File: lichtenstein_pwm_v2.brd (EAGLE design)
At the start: 71.9 x 117 mm, 94 parts, among them IC1 MAX11647, IC2 MCP23017, IC3 74AHCT125SOIC14, IC5 LM75B, IC9 LD1117, J1 MAGJACK, U1 ONION-OMEGA2

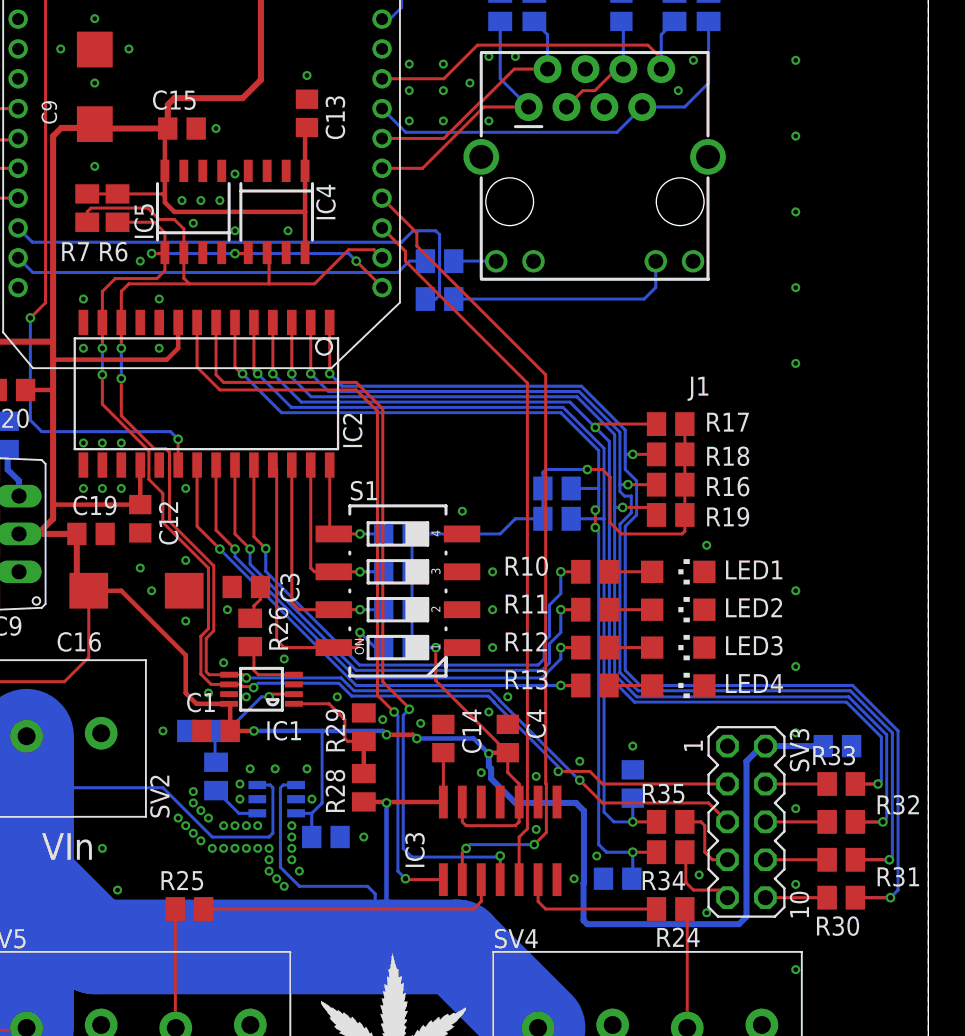
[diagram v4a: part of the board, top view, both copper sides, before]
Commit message: removed input connector, cleaned up some signals
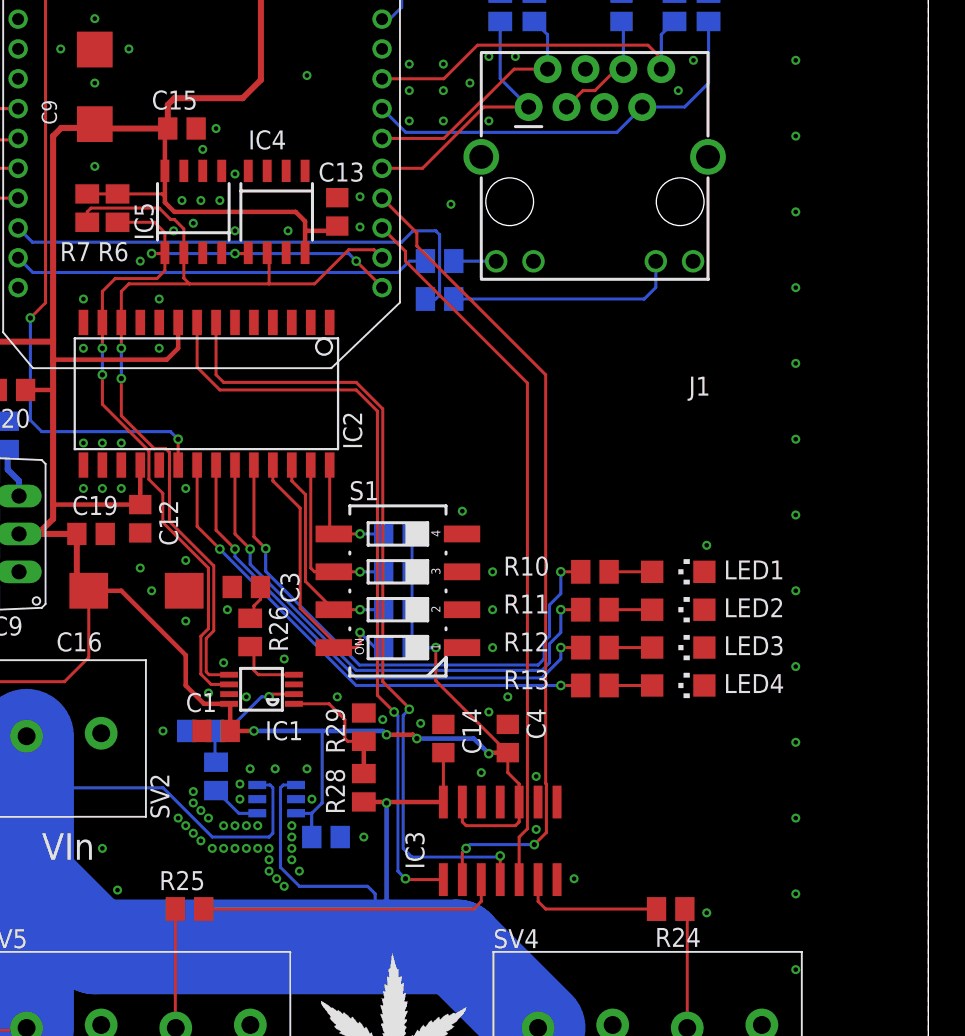
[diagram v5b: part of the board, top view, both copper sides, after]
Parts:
- removed C21, C22, C23, C24, C25, C26, C27: 100nF, rcl:C0805
- removed R16, R17, R18, R19, R20, R21, R30, R31, R32, R33, R34, R35: 10k, rcl:M0805
- removed SV3: (no value), con-lstb:MA05-2
- moved C13 6.91 mm to (32.3, 82.5)
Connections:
- removed net INPUT0: C21.2, IC2.2, R16.1, R31.2
- removed net INPUT1: C22.2, IC2.4, R17.1, R33.2
- removed net INPUT2: C23.2, IC2.6, R20.1, R34.2
- removed net INPUT3: C24.2, IC2.5, R21.1, R35.2
- removed net INPUT4: C25.2, IC2.1, R18.1, R30.2
- removed net INPUT5: C26.2, IC2.3, R19.1, R32.2
- removed net N$15: R30.1, SV3.10
- removed net N$16: R31.1, SV3.8
- removed net N$17: R32.1, SV3.6
- removed net N$18: R33.1, SV3.4
- removed net N$19: R34.1, SV3.9
- removed net N$20: R35.1, SV3.7
- net +3V3: no longer C27.2, IC4.1, R16.2, R17.2, R18.2, R19.2, R20.2, R21.2, SV3.2
- net GND: now also IC4.1; no longer C21.1, C22.1, C23.1, C24.1, C25.1, C26.1, C27.1, SV3.1
- net I2C_SCL: no longer SV3.5
- net I2C_SDA: no longer SV3.3
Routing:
- net +3V3: track 313.0 -> 232.8 mm, vias 6 -> 5
- net INPUT4: track 79.7 -> 0.00 mm, vias 3 -> 0
- net INPUT0: track 78.3 -> 0.00 mm, vias 3 -> 0
- net INPUT5: track 75.6 -> 0.00 mm, vias 3 -> 0
- net INPUT1: track 74.0 -> 0.00 mm, vias 3 -> 0
- net INPUT2: track 64.0 -> 0.00 mm, vias 4 -> 0
- net INPUT3: track 60.8 -> 0.00 mm, vias 2 -> 0
- net I2C_SCL: track 100.5 -> 63.0 mm, vias 4 -> 2
- net I2C_SDA: track 97.3 -> 60.7 mm, vias 7 -> 5
- net N$19: track 5.27 -> 0.00 mm
- net N$20: track 4.95 -> 0.00 mm
- net N$18: track 4.13 -> 0.00 mm
- net N$17: track 4.13 -> 0.00 mm
- net N$16: track 4.13 -> 0.00 mm
- net N$15: track 4.13 -> 0.00 mm
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
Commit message: more aesthetic fixes to board
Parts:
- moved C15 1.27 mm to (21.8, 89.4)
- moved C9 0.76 mm to (16.0, 91.7)
- moved R6 0.76 mm to (16.8, 82.8)
- moved R7 0.76 mm to (14.7, 82.8)
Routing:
- net +3V3: track 232.8 -> 231.4 mm
- net I2C_SDA: track 60.7 -> 61.4 mm
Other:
- board text added: "GND TX RX UART"

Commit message: more board clean-up
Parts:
- removed C28, C29, C30: 100nF, rcl:C0805
- removed R27: 1k2, rcl:M0805
- removed R28: 3k09, rcl:M0805
- removed R29: 1k07, rcl:M0805
- removed R36: 330R, rcl:M0805
- added C21, C24: 100nF, rcl:C0805
- added C22: 100µF, rcl:PANASONIC_D
- added C23: 100µF, rcl:CT7343
- added R16: 49.9R, rcl:M0805
- added R17, R18: 680R, rcl:M0805
- added R19: 330R, rcl:M0805
- added SV3: (no value), con-lstb:MA04-1
- C16: value 100µF -> 100nF; device rcl:CT7343 -> rcl:C0805
- C17: value 100µF -> 100nF; device rcl:PANASONIC_D -> rcl:C0805
- C4, C6: value 100nF -> 47µF; device rcl:C0805 -> rcl:SMC_C
- C5, C9: value 47µF -> 100nF; device rcl:SMC_C -> rcl:C0805
- IC1: value MAX11647 -> MCP23017; device lichtenstein_onion:UMAX8 -> lichtenstein_onion:SO28W
- IC2: value MCP23017 -> 74AHCT125SOIC14; device lichtenstein_onion:SO28W -> lichtenstein_onion:SO14
- IC3: value 74AHCT125SOIC14 -> MAX11647; device lichtenstein_onion:SO14 -> lichtenstein_onion:UMAX8
- R15: value 49.9R -> 1k2
- R22: value 680R -> 3k09
- R23: value 680R -> 1k07
- SV2: value 1792863 -> (none); device lichtenstein_onion:1792863 -> con-lstb:MA06-1
- SV6: value (none) -> 1792863; device con-lstb:MA06-1 -> lichtenstein_onion:1792863
- moved R15 79.5 mm to (5.33, 27.7), flipped to the top, turned to 180 degrees
- moved C7 78.2 mm to (44.2, 99.3), turned to 0 degrees
- moved C6 70.8 mm to (16.0, 91.7), flipped to the top, turned to 90 degrees
- moved C15 69.1 mm to (11.4, 21.1), flipped to the bottom, turned to 270 degrees
- moved C4 61.4 mm to (24.6, 105.7), turned to 180 degrees
- moved C3 50.0 mm to (40.1, 105.4)
- moved C11 49.6 mm to (43.7, 47.2), flipped to the top
- moved C16 44.9 mm to (45.5, 21.1), flipped to the bottom, turned to 270 degrees
- moved C10 44.3 mm to (10.4, 70.6), flipped to the top, turned to 180 degrees
- moved SV2 36.6 mm to (5.08, 83.6), turned to 90 degrees
- moved SV6 36.6 mm to (11.4, 47.5), turned to 0 degrees
- moved C14 36.0 mm to (32.3, 82.5)
- moved C13 35.7 mm to (24.1, 47.8), turned to 0 degrees
- moved R22 35.7 mm to (34.0, 43.9), flipped to the top, turned to 270 degrees
- moved IC2 35.5 mm to (43.2, 40.4), turned to 0 degrees
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- renumbered IC9 to IC7, R25 to R20, R26 to R21
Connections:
- net !PWM0_OE: now also IC1.8, IC2.1; no longer IC2.8, IC3.1
- net !PWM1_OE: now also IC1.7, IC2.4; no longer IC2.7, IC3.4
- net !SPI_CS: now also SV2.3; no longer SV6.3
- net +3V3: now also C1.1, C10.1, C11.2, C14.2, C18.2, C19.2, C23.+, C24.1, C3.1, C4.+, C6.+, C9.1, IC1.18, IC1.9, IC2.10, IC2.13, IC3.8, SV2.2, SV3.2; no longer C1.2, C12.1, C15.2, C16.+, C19.1, C20.1, C28.1, C29.2, C4.2, C5.+, C9.+, IC1.8, IC2.18, IC2.9, IC3.10, IC3.13, SV6.2
- net CURRENT: now also C20.1, IC3.2, R24.1; no longer C30.1, IC1.2, R36.1
- net ETH_CT: now also C8.2; no longer C11.2
- net ETH_LED_ACT: now also R17.2; no longer R22.2
- net ETH_LED_LINK: now also R18.2; no longer R23.2
- net ETH_RX-: now also R16.1; no longer R15.1
- net GND: now also C1.2, C10.2, C12.1, C15.2, C16.2, C17.1, C18.1, C19.1, C21.2, C22.-, C23.-, C24.2, C3.2, C4.-, C5.1, C6.-, C7.1, C9.2, IC1.10, IC1.15, IC1.16, IC1.17, IC2.12, IC2.7, IC2.9, R23.1, SV2.1, SV3.1, SV6.2; no longer C1.1, C10.1, C12.2, C15.1, C16.-, C17.-, C18.2, C19.2, C28.2, C29.1, C3.1, C30.2, C4.1, C5.-, C6.2, C7.2, C9.-, IC1.7, IC2.10, IC2.15, IC2.16, IC2.17, IC3.12, IC3.9, R29.1, SV2.2, SV6.1
- net I2C_INT: now also IC1.20; no longer IC2.20
- net I2C_SCL: now also IC1.12, IC3.5, SV3.3; no longer IC1.5, IC2.12
- net I2C_SDA: now also IC1.13, IC3.6, SV3.4; no longer IC1.6, IC2.13
- net N$12: now also IC3.4; no longer IC1.4
- net N$13: now also C17.2; no longer C3.2
- net N$14: now also R15.2; no longer R27.2
- net N$21: now also R24.2; no longer R36.2
- net N$3: now also C5.2; no longer C8.2
- net N$4: now also R17.1; no longer R22.1
- net N$5: now also R18.1; no longer R23.1
- net N$6: now also C7.2, R16.2; no longer C10.2, R15.2
- net N$7: now also R19.2; no longer R24.2
- net PWM0: now also IC2.2; no longer IC3.2
- net PWM1: now also IC2.5; no longer IC3.5
- net PWMOUT0: now also IC2.6, R19.1; no longer IC3.6, R24.1
- net PWMOUT1: now also IC2.3; no longer IC3.3
- net SPI_MISO: now also SV2.6; no longer SV6.6
- net SPI_MOSI: now also SV2.5; no longer SV6.5
- net SPI_SCK: now also SV2.4; no longer SV6.4
- net STATUS0: now also IC1.24; no longer IC2.24
- net STATUS1: now also IC1.23; no longer IC2.23
- net STATUS2: now also IC1.22; no longer IC2.22
- net STATUS3: now also IC1.21; no longer IC2.21
- net TEST0: now also IC1.25; no longer IC2.25
- net TEST1: now also IC1.26; no longer IC2.26
- net TEST2: now also IC1.27; no longer IC2.27
- net TEST3: now also IC1.28; no longer IC2.28
- net V+: now also C12.2, C15.1, C16.1, C21.1, C22.+, IC2.14, R15.1, R22.2, SV6.1; no longer C14.2, C17.+, C18.1, C6.1, C7.1, IC3.14, R27.1, R28.2, SV2.1
- net VIN_DIVIDED: now also IC3.1, R22.1, R23.2; no longer IC1.1, R28.1, R29.2
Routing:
- net +3V3: track 231.4 -> 270.6 mm, vias 5 -> 7
- net I2C_SCL: track 63.4 -> 98.2 mm, vias 2 -> 3
- net I2C_SDA: track 61.4 -> 93.2 mm
- net ETH_LED_LINK: track 34.2 -> 33.1 mm

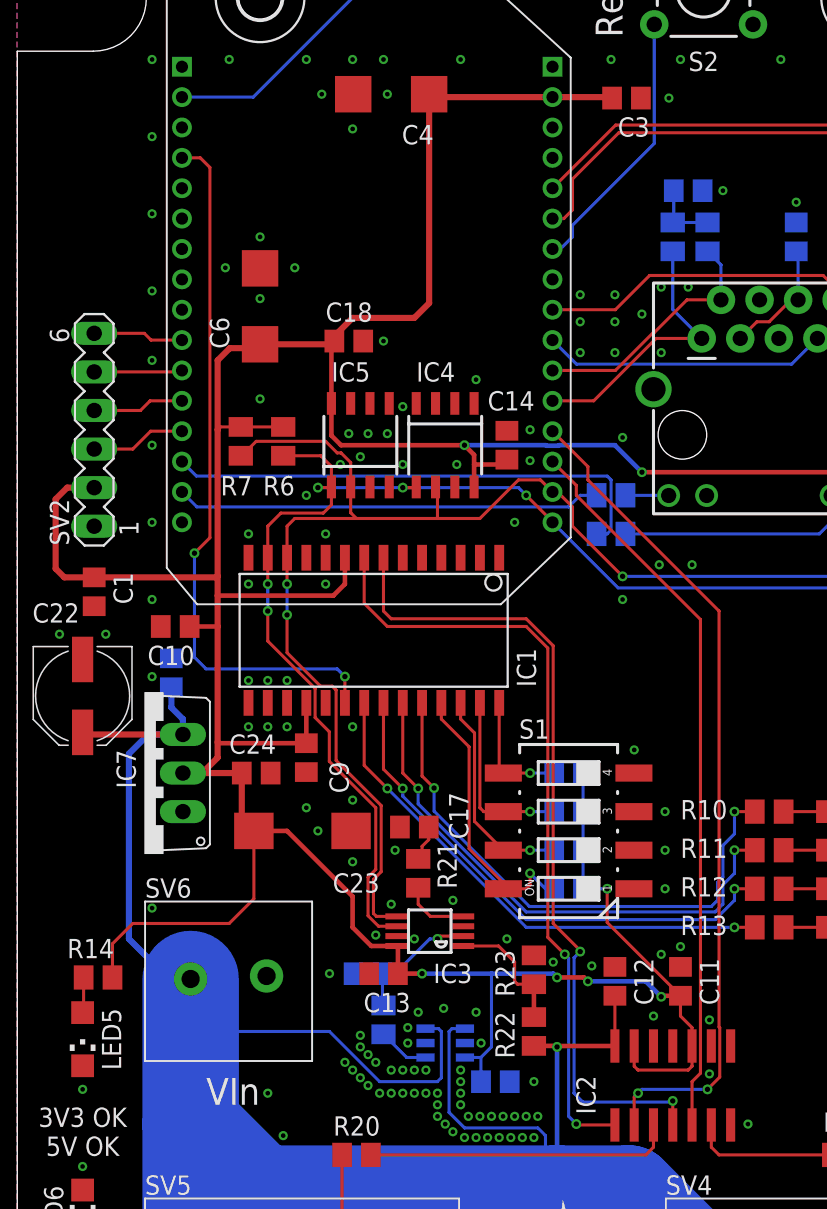
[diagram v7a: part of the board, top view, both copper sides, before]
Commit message: moved i2c expander more underneath omega module
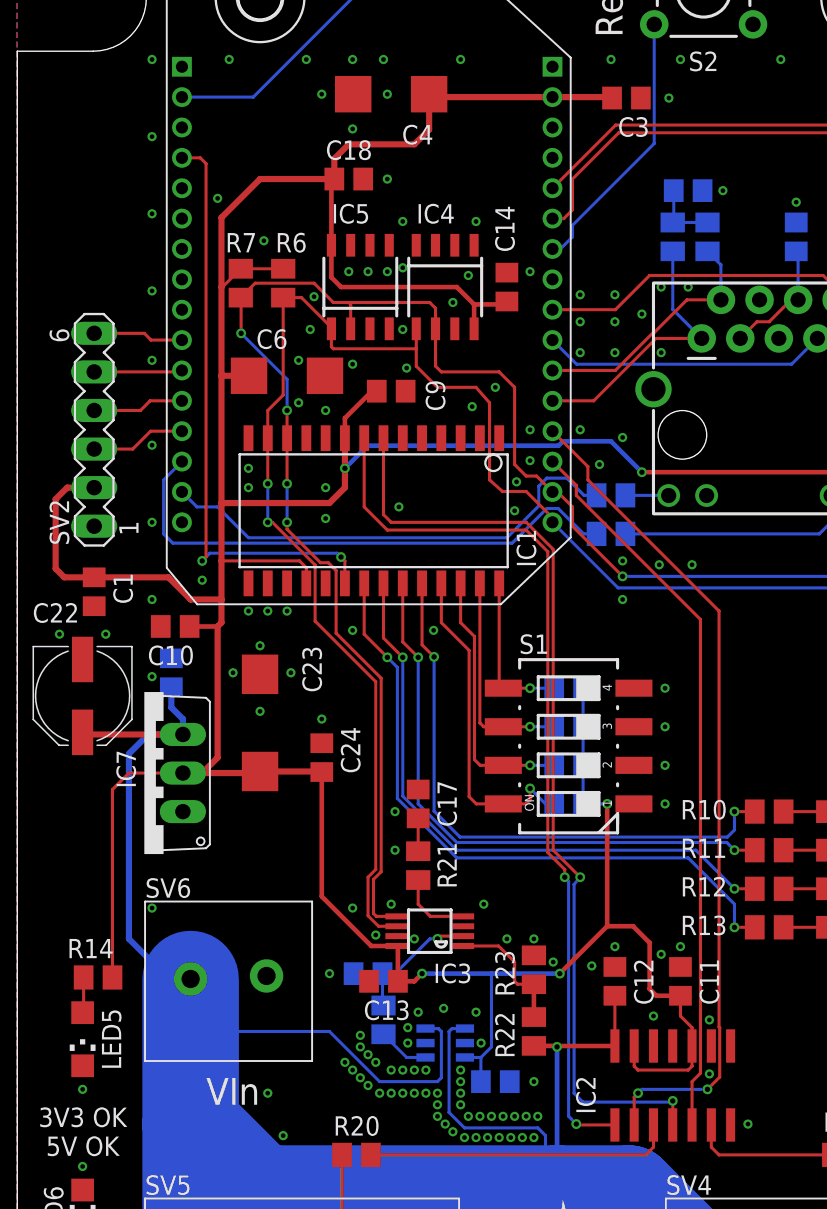
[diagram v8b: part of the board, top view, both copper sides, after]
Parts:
- moved C9 24.8 mm to (24.6, 86.1), turned to 0 degrees
- moved C18 10.7 mm to (21.8, 100.1)
- moved C14 10.4 mm to (32.3, 93.0)
- moved IC4 10.4 mm to (28.2, 93.0)
- moved IC5 10.4 mm to (22.6, 93.0)
- moved R6 10.4 mm to (17.5, 93.2)
- moved R7 10.4 mm to (14.7, 93.2)
- moved IC1 7.87 mm to (24.1, 78.2)
- moved C23 7.64 mm to (16.0, 64.3), turned to 90 degrees
- moved R2 5.59 mm to (36.3, 61.5)
- moved R4 5.59 mm to (36.3, 66.5)
- moved S1 5.59 mm to (36.3, 62.7)
- moved R1 5.59 mm to (36.3, 58.9)
- moved R3 5.59 mm to (36.3, 64.0)
- moved C6 4.91 mm to (17.8, 87.1), turned to 0 degrees
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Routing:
- net +3V3: track 270.6 -> 291.4 mm, vias 7 -> 5
- net I2C_SCL: track 98.2 -> 114.7 mm, vias 3 -> 5
- net I2C_SDA: track 93.2 -> 109.2 mm, vias 5 -> 2
- net STATUS3: track 34.2 -> 43.0 mm
- net !PWM0_OE: track 51.0 -> 58.9 mm
- net !PWM1_OE: track 54.4 -> 62.2 mm
- net I2C_INT: track 46.9 -> 39.3 mm
- net STATUS2: track 34.5 -> 40.2 mm
- net ETH_LED_ACT: track 28.0 -> 31.4 mm
- net TEST0: track 18.6 -> 21.9 mm
- net TEST1: track 14.2 -> 17.4 mm
- net STATUS1: track 35.5 -> 38.4 mm
- net ETH_LED_LINK: track 33.1 -> 35.7 mm
- net TEST2: track 11.9 -> 14.2 mm
- net TEST3: track 8.08 -> 10.4 mm
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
